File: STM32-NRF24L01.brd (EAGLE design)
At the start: 45 x 23 mm, 5 parts, among them IC1 STM32F030K6T6

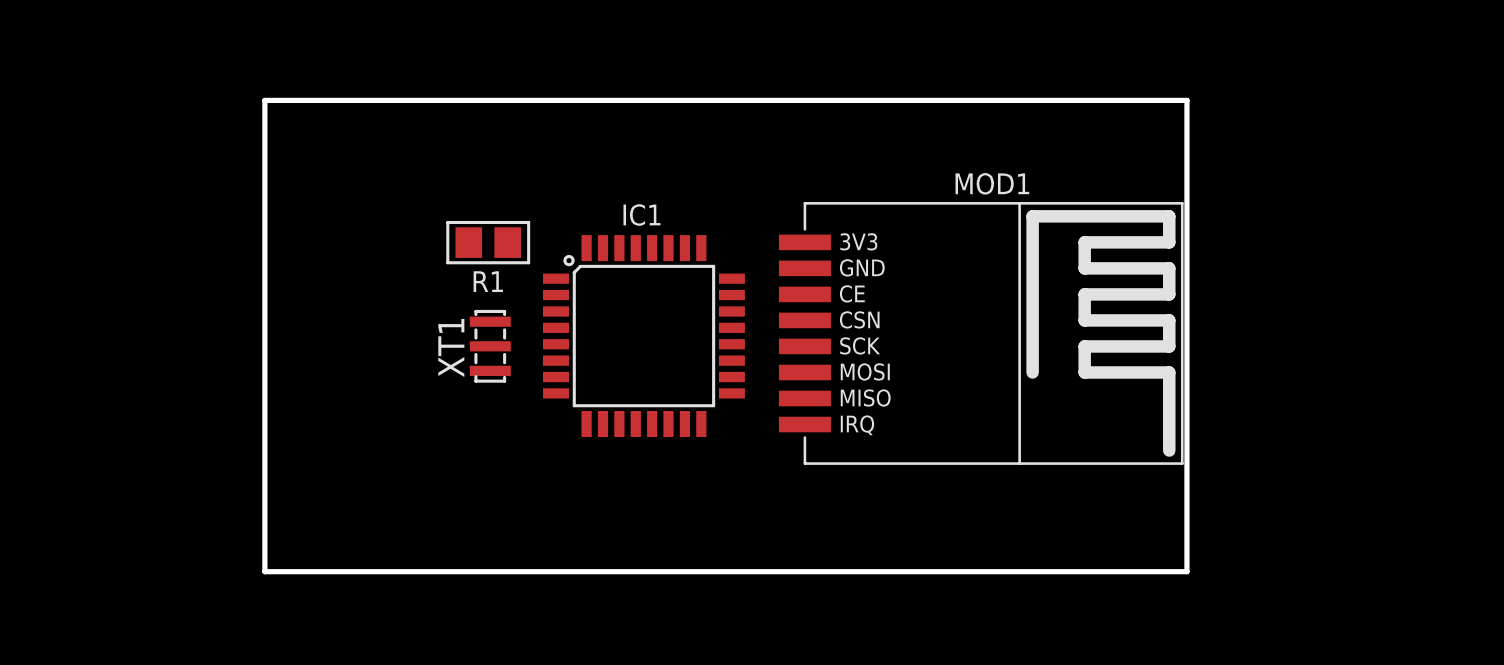
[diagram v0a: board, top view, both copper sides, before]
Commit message: Add conectores y circuiteria basica para el STM32
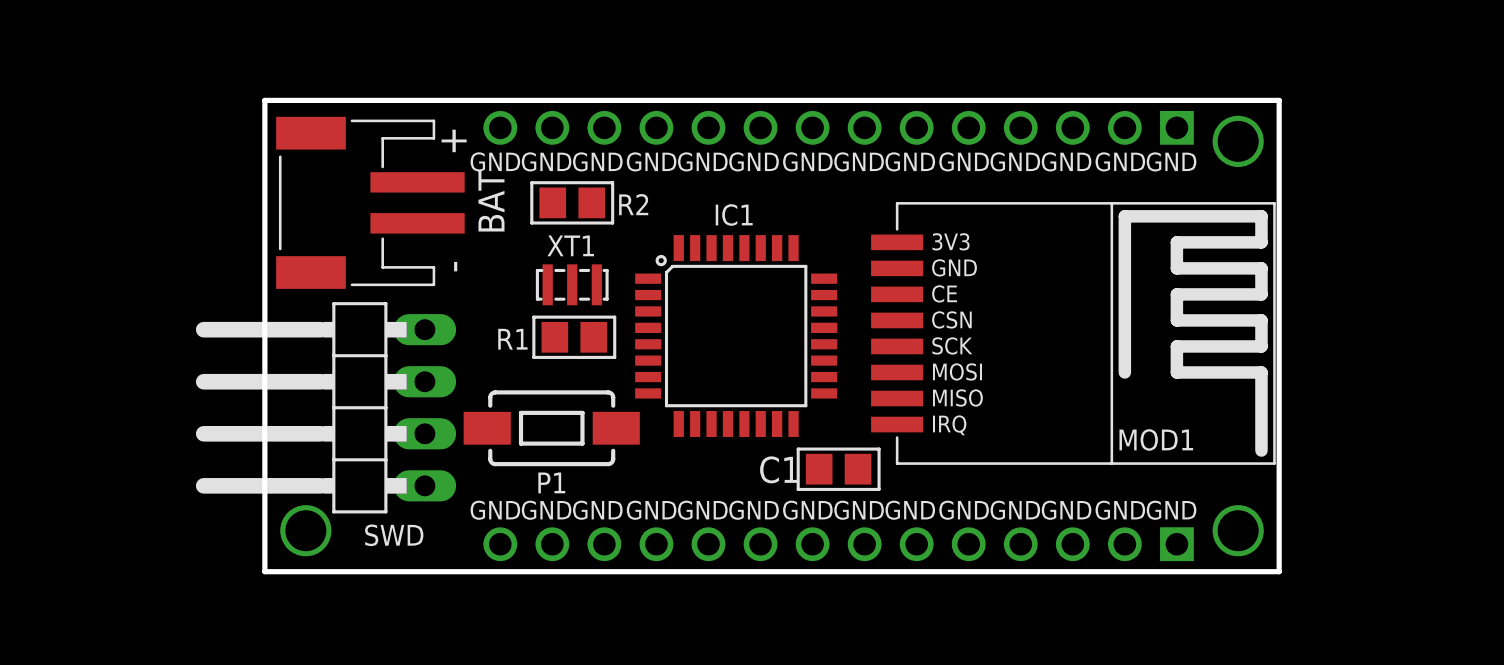
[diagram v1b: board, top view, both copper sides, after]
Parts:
- added BAT: JST-2PIN-PH-SM4, CaliBeta-Conectores:S2B-PH-SM4
- added C1: 100nF, CaliBeta-RCL:C0805
- added J1, J2: 61301411121, Headers:61301411121
- added P1: PUSH-SMD, CaliBeta-Miselaneos:ST-SMD-6X3.5MM
- added R2: 10k, CaliBeta-RCL:R0805
- added SWD: (no value), pinhead:1X04/90
- moved R1 6.24 mm to (15.1, 11.4), turned to 0 degrees
- moved XT1 5.00 mm to (15.0, 14.0), turned to 0 degrees
- moved IC1 4.50 mm to (23.0, 11.5)
- moved MOD1 4.50 mm to (40.0, 11.5)
- moved U$1 4.00 mm to (26.5, 11.5)
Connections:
- removed net NRST: IC1.4, R1.2
- removed net VDDA: IC1.5
- new net RST: IC1.4, P1.2, R1.2
- net +3V3: now also C1.1, IC1.5, SWD.1
- net BOOT0: now also R2.2
- net GND: now also C1.2, J1.14, J2.14, P1.1, R2.1, SWD.4
- net SWCLK: now also SWD.3
- net SWDIO: now also SWD.2
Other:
- board size 45 x 23 mm -> 49.5 x 23 mm
- board text added: "GND"

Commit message: Add cargador de bateria
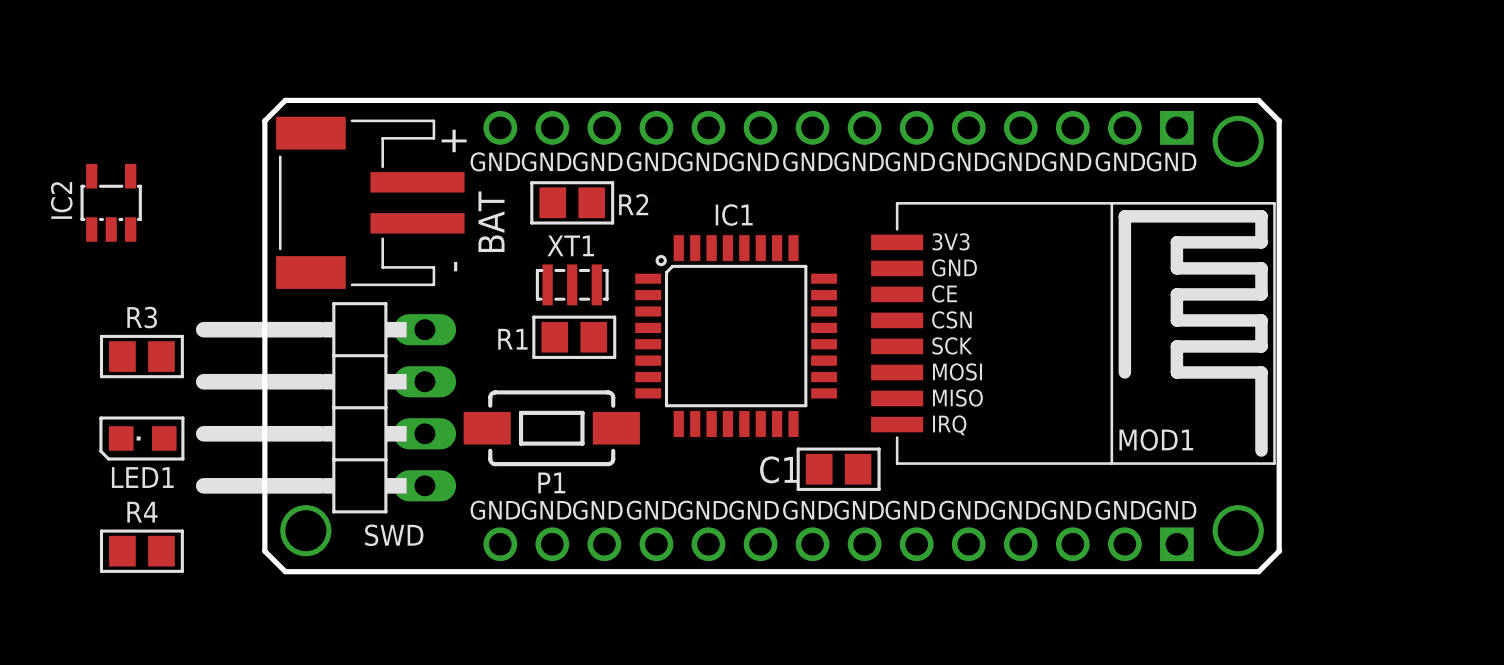
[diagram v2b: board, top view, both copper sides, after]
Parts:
- added IC2: MCP73811/2, adafruit:SOT23-5L
- added LED1: (no value), CaliBeta-Diodos:LED0805-ROJO
- added R3: 1k, CaliBeta-RCL:R0805
- added R4: 10k, CaliBeta-RCL:R0805
- BAT: value JST-2PIN-PH-SM4 -> 3.7V
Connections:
- new net +5V: IC2.4, LED1.A
- new net N$7: LED1.C, R3.1
- new net N$8: IC2.5, R4.1
- new net STAT: IC2.1, R3.2
- new net V+: BAT.1, IC2.3
- net GND: now also BAT.2, IC2.2, R4.2
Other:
- outline, holes or cut-outs redrawn
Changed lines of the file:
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@@
 <board>
 <plain>
-<wire x1="0" y1="0" x2="49.5" y2="0" width="0.254" layer="20"/>
-<wire x1="49.5" y1="0" x2="49.5" y2="23" width="0.254" layer="20"/>
-<wire x1="49.5" y1="23" x2="0" y2="23" width="0.254" layer="20"/>
-<wire x1="0" y1="23" x2="0" y2="0" width="0.254" layer="20"/>
+<wire x1="1" y1="0" x2="48.5" y2="0" width="0.254" layer="20"/>
+<wire x1="49.5" y1="1" x2="49.5" y2="22" width="0.254" layer="20"/>
+<wire x1="48.5" y1="23" x2="1" y2="23" width="0.254" layer="20"/>
 <text x="11.25" y="3" size="0.9" layer="21" font="vector" ratio="12" align="center">GND</text>
 <text x="13.75" y="3" size="0.9" layer="21" font="vector" ratio="12" align="center">GND</text>
@@
 <text x="41.75" y="20" size="0.9" layer="21" font="vector" ratio="12" align="center">GND</text>
 <text x="44.25" y="20" size="0.9" layer="21" font="vector" ratio="12" align="center">GND</text>
+<wire x1="0" y1="22" x2="0" y2="1" width="0.254" layer="20"/>
+<wire x1="49.5" y1="22" x2="48.5" y2="23" width="0.254" layer="20"/>
+<wire x1="49.5" y1="1" x2="48.5" y2="0" width="0.254" layer="20"/>
+<wire x1="0" y1="1" x2="1" y2="0" width="0.254" layer="20"/>
+<wire x1="1" y1="23" x2="0" y2="22" width="0.254" layer="20"/>
 </plain>
 <attributes>
@@
 <attribute name="VALUE" x="14.966" y="12.137" size="1.27" layer="27" align="center"/>
 </element>
-<element name="BAT" library="CaliBeta-Conectores" library_urn="urn:adsk.eagle:library:14344905" package="S2B-PH-SM4" package3d_urn="urn:adsk.eagle:package:24309458/2" value="JST-2PIN-PH-SM4" x="3.75" y="18" smashed="yes" rot="R90">
-<attribute name="NAME" x="11.059" y="18" size="1.27" layer="25" font="vector" ratio="10" rot="R90" align="center"/>
+<element name="BAT" library="CaliBeta-Conectores" library_urn="urn:adsk.eagle:library:14344905" package="S2B-PH-SM4" package3d_urn="urn:adsk.eagle:package:24309458/2" value="3.7V" x="3.75" y="18" smashed="yes" rot="R90">
+<attribute name="NAME" x="11.059" y="17" size="1.27" layer="25" font="vector" ratio="10" rot="R90" align="center"/>
 <attribute name="VALUE" x="11.37" y="18" size="1.27" layer="27" font="vector" rot="R90" align="center"/>
 </element>
@@
 <attribute name="NAME" x="46.08" y="23.66" size="1.016" layer="26" ratio="12" rot="MR0"/>
 <attribute name="VALUE" x="46.08" y="17.66" size="1.778" layer="28" rot="MR0"/>
+</element>
+<element name="IC2" library="adafruit" library_urn="urn:adsk.eagle:library:420" package="SOT23-5L" package3d_urn="urn:adsk.eagle:package:6240724/1" value="MCP73811/2" x="-7.5" y="18" smashed="yes">
+<attribute name="NAME" x="-9.405" y="17.095" size="1.016" layer="25" ratio="12" rot="R90"/>
+<attribute name="VALUE" x="-9.405" y="14.571" size="1.27" layer="27"/>
+</element>
+<element name="R3" library="CaliBeta-RCL" library_urn="urn:adsk.eagle:library:14345719" package="R0805" package3d_urn="urn:adsk.eagle:package:14345749/1" value="1k" x="-6" y="10.5" smashed="yes">
+<attribute name="NAME" x="-6" y="12.405" size="1.016" layer="25" ratio="12" align="center"/>
+<attribute name="VALUE" x="-6" y="8.595" size="1.27" layer="27" align="center"/>
+</element>
+<element name="LED1" library="CaliBeta-Diodos" library_urn="urn:adsk.eagle:library:14345451" package="LED0805-ROJO" package3d_urn="urn:adsk.eagle:package:14345485/3" value="" x="-6" y="6.5" smashed="yes">
+<attribute name="NAME" x="-5.96" y="4.595" size="1.016" layer="25" ratio="12" rot="R180" align="center"/>
+<attribute name="VALUE" x="-5.96" y="8.405" size="1.27" layer="27" rot="R180" align="center"/>
+</element>
+<element name="R4" library="CaliBeta-RCL" library_urn="urn:adsk.eagle:library:14345719" package="R0805" package3d_urn="urn:adsk.eagle:package:14345749/1" value="10k" x="-6" y="1" smashed="yes">
+<attribute name="NAME" x="-6" y="2.905" size="1.016" layer="25" ratio="12" align="center"/>
+<attribute name="VALUE" x="-6" y="-0.905" size="1.27" layer="27" align="center"/>
 </element>
 </elements>
@@
 <contactref element="J1" pad="14"/>
 <contactref element="J2" pad="14"/>
+<contactref element="R4" pad="2"/>
+<contactref element="IC2" pad="2"/>
+<contactref element="BAT" pad="2"/>
 <wire x1="25.8" y1="7.2074" x2="30.856" y2="14.802" width="0" layer="19" extent="1-1"/>
 <wire x1="27.05" y1="5" x2="25.8" y2="7.2074" width="0" layer="19" extent="1-1"/>
@@
 <wire x1="11.49" y1="21.66" x2="14.05" y2="18" width="0" layer="19" extent="1-1"/>
 <wire x1="20.2" y1="15.7926" x2="15" y2="14" width="0" layer="19" extent="1-1"/>
-<wire x1="7.81" y1="11.81" x2="15" y2="14" width="0" layer="19" extent="1-1"/>
+<wire x1="7.45" y1="17" x2="11.49" y2="21.66" width="0" layer="19" extent="1-1"/>
+<wire x1="7.81" y1="11.81" x2="7.45" y2="17" width="0" layer="19" extent="1-1"/>
 <wire x1="11.49" y1="1.34" x2="17.15" y2="7" width="0" layer="19" extent="1-1"/>
+<wire x1="-7.5" y1="16.7" x2="11.49" y2="1.34" width="0" layer="19" extent="1-1"/>
+<wire x1="-5.05" y1="1" x2="-7.5" y2="16.7" width="0" layer="19" extent="1-1"/>
 </signal>
 <signal name="CE">
@@
 <via x="2" y="2" extent="1-16" drill="2"/>
 </signal>
+<signal name="N$7">
+<contactref element="R3" pad="1"/>
+<contactref element="LED1" pad="C"/>
+<wire x1="-6.95" y1="10.5" x2="-7.01" y2="6.5" width="0" layer="19" extent="1-1"/>
+</signal>
+<signal name="+5V">
+<contactref element="IC2" pad="4"/>
+<contactref element="LED1" pad="A"/>
+<wire x1="-6.55" y1="19.3" x2="-4.91" y2="6.5" width="0" layer="19" extent="1-1"/>
+</signal>
+<signal name="N$8">
+<contactref element="IC2" pad="5"/>
+<contactref element="R4" pad="1"/>
+<wire x1="-8.45" y1="19.3" x2="-6.95" y2="1" width="0" layer="19" extent="1-1"/>
+</signal>
+<signal name="V+">
+<contactref element="IC2" pad="3"/>
+<contactref element="BAT" pad="1"/>
+<wire x1="-6.55" y1="16.7" x2="7.45" y2="19" width="0" layer="19" extent="1-1"/>
+</signal>
+<signal name="STAT">
+<contactref element="IC2" pad="1"/>
+<contactref element="R3" pad="2"/>
+<wire x1="-8.45" y1="16.7" x2="-5.05" y2="10.5" width="0" layer="19" extent="1-1"/>
+</signal>
 </signals>

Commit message: Add Regulador 3V3
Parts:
- added C2, C3: 10uF, CaliBeta-RCL:C0805
- added D1: SS14, CaliBeta-Diodos:DO-214AC
- added IC3: SPX3819M5_3_3, SparkFun-IC-Power:SOT23-5
- added R5: 1k, CaliBeta-RCL:R0805
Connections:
- new net EN: IC3.3, R5.2
- net +3V3: now also C3.1, IC3.5
- net +5V: now also C2.1, D1.K, IC3.1, R5.1
- net GND: now also C2.2, C3.2, IC3.2
- net V+: now also D1.A
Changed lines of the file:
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@@
 <attribute name="VALUE" x="-6" y="-0.905" size="1.27" layer="27" align="center"/>
+</element>
+<element name="IC3" library="SparkFun-IC-Power" library_urn="urn:adsk.eagle:library:526" package="SOT23-5" package3d_urn="urn:adsk.eagle:package:39060/1" value="SPX3819M5_3_3" x="53.5" y="24" smashed="yes">
+<attribute name="NAME" x="51.341" y="24.111" size="1.016" layer="25" ratio="12" rot="R90" align="center"/>
+<attribute name="PROD_ID" value="VREG-13321" x="53.5" y="24" size="1.016" layer="27" font="vector" ratio="12" display="off"/>
+<attribute name="VALUE" x="52.5475" y="23.8095" size="0.4064" layer="27"/>
+</element>
+<element name="D1" library="CaliBeta-Diodos" library_urn="urn:adsk.eagle:library:14345451" package="DO-214AC" package3d_urn="urn:adsk.eagle:package:14345492/2" value="SS14" x="55.5" y="18" smashed="yes">
+<attribute name="NAME" x="55.527" y="20.173" size="1.016" layer="25" ratio="12" align="center"/>
+<attribute name="VALUE" x="55.527" y="15.829" size="1.27" layer="27" ratio="10" align="center"/>
+</element>
+<element name="C2" library="CaliBeta-RCL" library_urn="urn:adsk.eagle:library:14345719" package="C0805" package3d_urn="urn:adsk.eagle:package:14345754/1" value="10uF" x="55.5" y="11.5" smashed="yes">
+<attribute name="NAME" x="55.5" y="13.405" size="1.016" layer="25" ratio="12" align="center"/>
+<attribute name="VALUE" x="55.5" y="9.595" size="1.27" layer="27" align="center"/>
+</element>
+<element name="C3" library="CaliBeta-RCL" library_urn="urn:adsk.eagle:library:14345719" package="C0805" package3d_urn="urn:adsk.eagle:package:14345754/1" value="10uF" x="55.5" y="5" smashed="yes">
+<attribute name="NAME" x="55.5" y="6.905" size="1.016" layer="25" ratio="12" align="center"/>
+<attribute name="VALUE" x="55.5" y="3.095" size="1.27" layer="27" align="center"/>
+</element>
+<element name="R5" library="CaliBeta-RCL" library_urn="urn:adsk.eagle:library:14345719" package="R0805" package3d_urn="urn:adsk.eagle:package:14345749/1" value="1k" x="55.5" y="-1.5" smashed="yes">
+<attribute name="NAME" x="55.5" y="0.405" size="1.016" layer="25" ratio="12" align="center"/>
+<attribute name="VALUE" x="55.5" y="-3.405" size="1.27" layer="27" align="center"/>
 </element>
 </elements>
@@
 <contactref element="C1" pad="1"/>
 <contactref element="IC1" pad="5"/>
+<contactref element="IC3" pad="5"/>
+<contactref element="C3" pad="1"/>
 <wire x1="27.2926" y1="8.7" x2="30.856" y2="16.072" width="0" layer="19" extent="1-1"/>
 <wire x1="28.95" y1="5" x2="27.2926" y2="8.7" width="0" layer="19" extent="1-1"/>
@@
 <wire x1="14.15" y1="11.44" x2="18.7074" y2="11.1" width="0" layer="19" extent="1-1"/>
 <wire x1="7.81" y1="4.19" x2="14.15" y2="11.44" width="0" layer="19" extent="1-1"/>
+<wire x1="52.55" y1="25.3001" x2="7.81" y2="4.19" width="0" layer="19" extent="1-1"/>
+<wire x1="54.55" y1="5" x2="52.55" y2="25.3001" width="0" layer="19" extent="1-1"/>
 </signal>
 <signal name="AN0">
@@
 <contactref element="IC2" pad="2"/>
 <contactref element="BAT" pad="2"/>
+<contactref element="C2" pad="2"/>
+<contactref element="C3" pad="2"/>
+<contactref element="IC3" pad="2"/>
 <wire x1="25.8" y1="7.2074" x2="30.856" y2="14.802" width="0" layer="19" extent="1-1"/>
 <wire x1="27.05" y1="5" x2="25.8" y2="7.2074" width="0" layer="19" extent="1-1"/>
@@
 <wire x1="7.81" y1="11.81" x2="7.45" y2="17" width="0" layer="19" extent="1-1"/>
 <wire x1="11.49" y1="1.34" x2="17.15" y2="7" width="0" layer="19" extent="1-1"/>
-<wire x1="-7.5" y1="16.7" x2="11.49" y2="1.34" width="0" layer="19" extent="1-1"/>
+<wire x1="-7.5" y1="16.7" x2="7.45" y2="17" width="0" layer="19" extent="1-1"/>
 <wire x1="-5.05" y1="1" x2="-7.5" y2="16.7" width="0" layer="19" extent="1-1"/>
+<wire x1="53.5" y1="22.6999" x2="-5.05" y2="1" width="0" layer="19" extent="1-1"/>
+<wire x1="56.45" y1="11.5" x2="53.5" y2="22.6999" width="0" layer="19" extent="1-1"/>
+<wire x1="56.45" y1="5" x2="56.45" y2="11.5" width="0" layer="19" extent="1-1"/>
 </signal>
 <signal name="CE">
@@
 <contactref element="IC2" pad="4"/>
 <contactref element="LED1" pad="A"/>
+<contactref element="D1" pad="K"/>
+<contactref element="IC3" pad="1"/>
+<contactref element="C2" pad="1"/>
+<contactref element="R5" pad="1"/>
+<wire x1="54.55" y1="11.5" x2="54.55" y2="-1.5" width="0" layer="19" extent="1-1"/>
+<wire x1="53.45" y1="18" x2="54.55" y2="11.5" width="0" layer="19" extent="1-1"/>
+<wire x1="52.55" y1="22.6999" x2="53.45" y2="18" width="0" layer="19" extent="1-1"/>
+<wire x1="-4.91" y1="6.5" x2="52.55" y2="22.6999" width="0" layer="19" extent="1-1"/>
 <wire x1="-6.55" y1="19.3" x2="-4.91" y2="6.5" width="0" layer="19" extent="1-1"/>
 </signal>
@@
 <contactref element="IC2" pad="3"/>
 <contactref element="BAT" pad="1"/>
+<contactref element="D1" pad="A"/>
 <wire x1="-6.55" y1="16.7" x2="7.45" y2="19" width="0" layer="19" extent="1-1"/>
+<wire x1="57.55" y1="18" x2="-6.55" y2="16.7" width="0" layer="19" extent="1-1"/>
 </signal>
 <signal name="STAT">
@@
 <wire x1="-8.45" y1="16.7" x2="-5.05" y2="10.5" width="0" layer="19" extent="1-1"/>
 </signal>
+<signal name="EN">
+<contactref element="IC3" pad="3"/>
+<contactref element="R5" pad="2"/>
+<wire x1="54.45" y1="22.6999" x2="56.45" y2="-1.5" width="0" layer="19" extent="1-1"/>
+</signal>
 </signals>
